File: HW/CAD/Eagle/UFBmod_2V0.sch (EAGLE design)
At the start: 67 parts, among them U301 MAX5217, U401 AT86RF215-ZU, U411 ASVTX-13-D-26.000MHZ-I05-T, U511 PE4259, U521 RFX1010, U581 B39871B3440U410, X1 TTE_EN11-HSM, X591 ANTENNATINY, X595 ANTENNATINY, X711 MOLEX 105017-0001, X721 PHOENIX_1990067_1X8X2MM50_PTS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, X722 PHOENIX_1990067_1X8X2MM50_PTS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, X723 PHOENIX_1990067_1X8X2MM50_PTS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

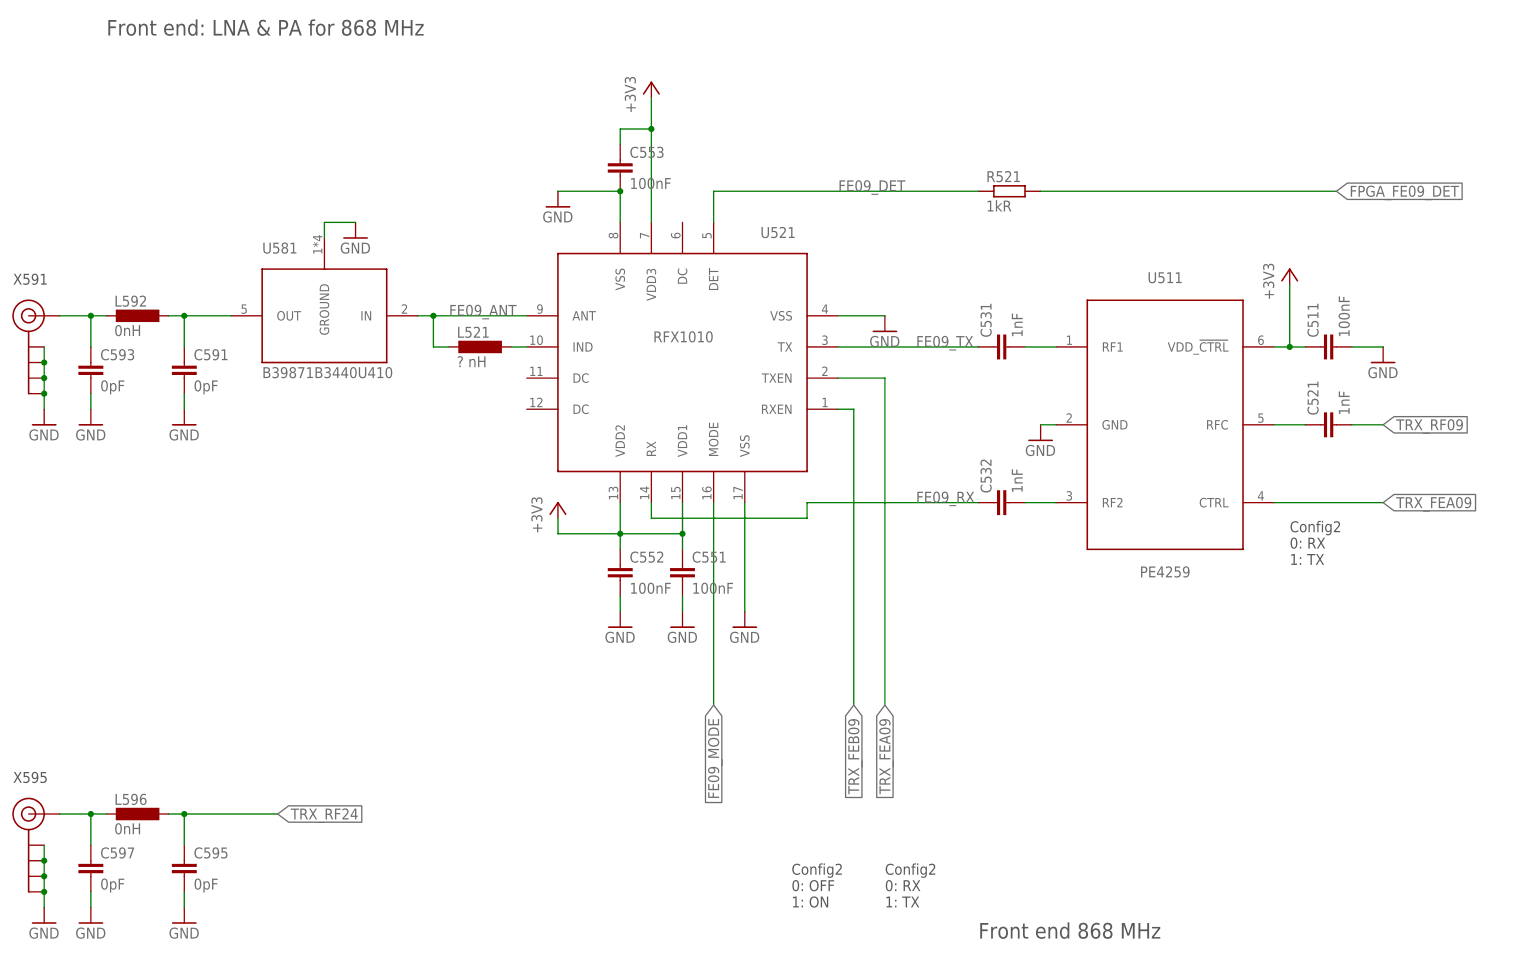
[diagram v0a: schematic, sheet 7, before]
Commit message: HW_2V0 - HW/CAD/Eagle - RFX1010 application schematic adapted
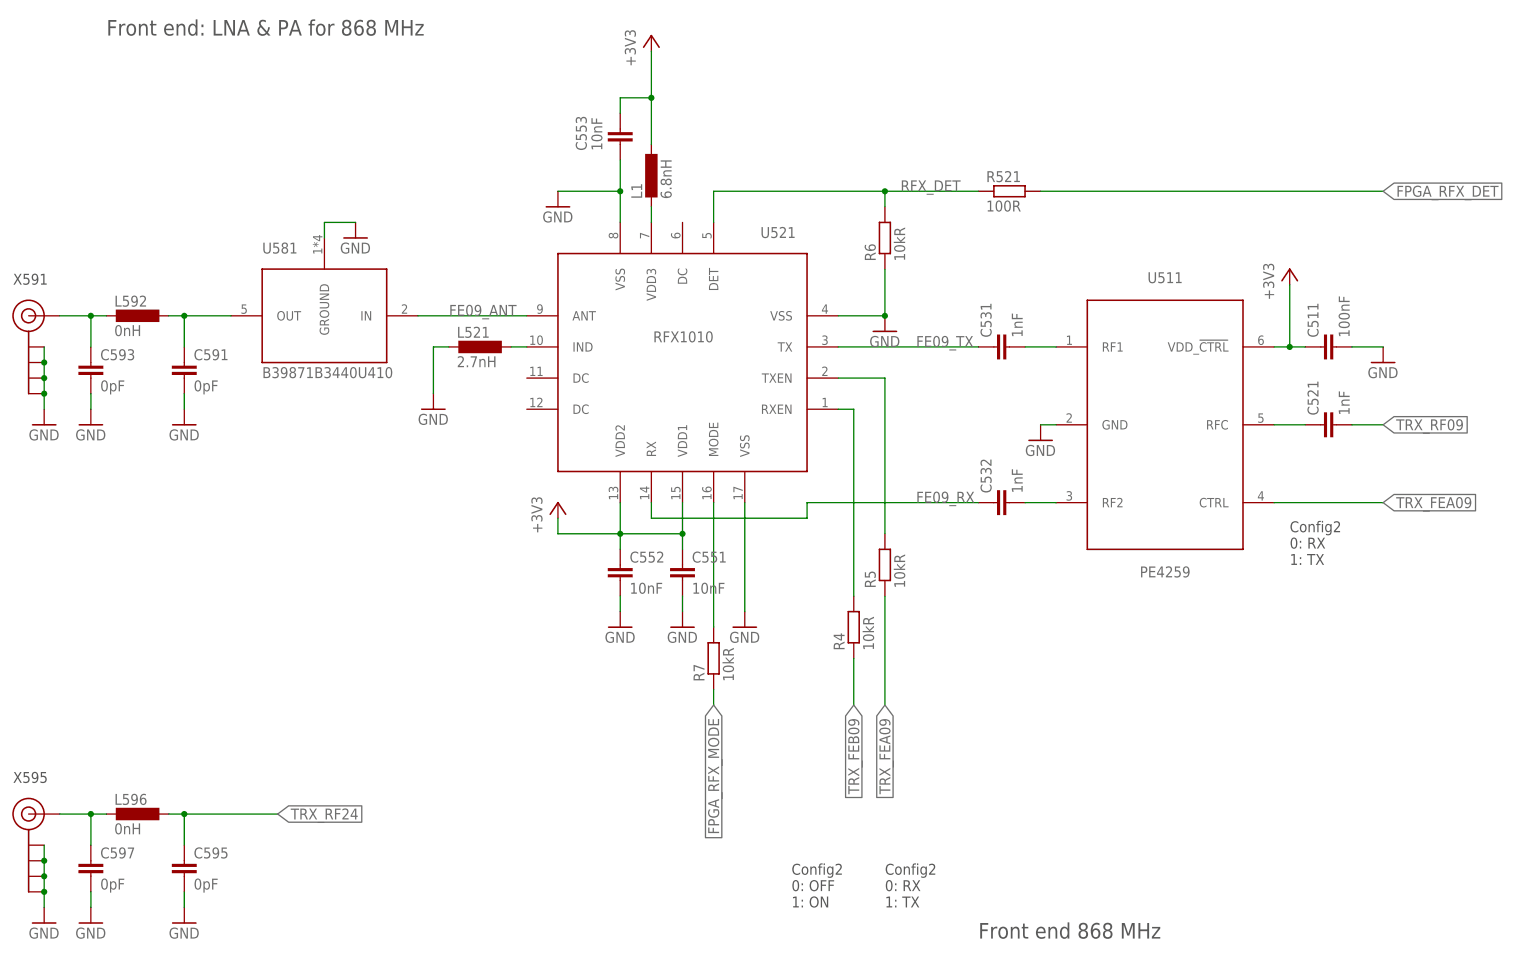
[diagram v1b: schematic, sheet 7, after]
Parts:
- added L1: 6.8nH, df4iah_rcl:L-EUL0603
- added R4, R5, R6, R7: 10kR, df4iah_rcl:R-EU_R0402
- C551, C552, C553: value 100nF -> 10nF
- L521: value ? nH -> 2.7nH
- R521: value 1kR -> 100R
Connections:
- net FE09_IND renamed RFX_IND
- net FPGA_FE09_DET renamed FPGA_RFX_DET
- removed net FE09_DET: R521.1, U521.DET
- removed net FE09_MODE: U521.MODE
- new net FPGA_RFX_MODE: R7.1
- new net RFX_DET: R521.1, R6.2, U521.DET
- new net RFX_MODE: R7.2, U521.MODE
- new net RFX_RXEN: R4.2, U521.RXEN
- new net RFX_TXEN: R5.2, U521.TXEN
- new net RFX_VDD3: L1.2, U521.VDD3
- net +3V3: now also L1.1; no longer U521.VDD3
- net FE09_ANT: no longer L521.2
- net GND: now also L521.2, R6.1
- net TRX_FEA09: now also R5.1; no longer U521.TXEN
- net TRX_FEB09: now also R4.1; no longer U521.RXEN
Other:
- note added: "SAMTEC LSHM-130-04.0-L-DV-A-S-K-TR 60 POS"
- note added: "SAMTEC LSHM-150-04.0-L-DV-A-S-K-TR 100 POS"
- moved on the sheet: C553

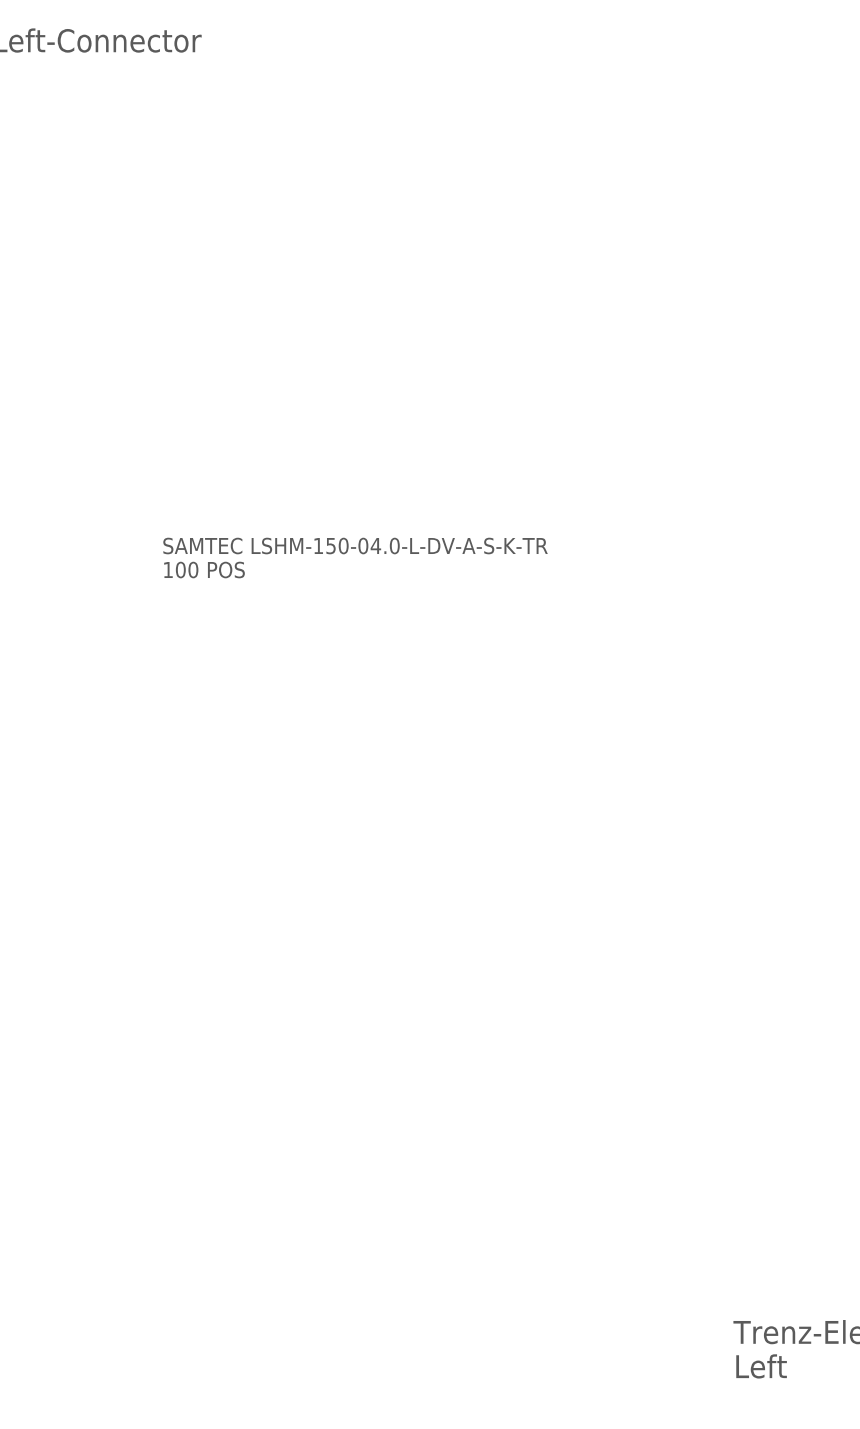
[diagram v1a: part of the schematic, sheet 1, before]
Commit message: HW_2V0 - HW/CAD/Eagle/lbr - df4iah_connector.lbr SEMTEC LSHM-150-02.5-L-DV-A-S-K-TR and LSHM-130-02.5-L-DV-A-S-K-TR added
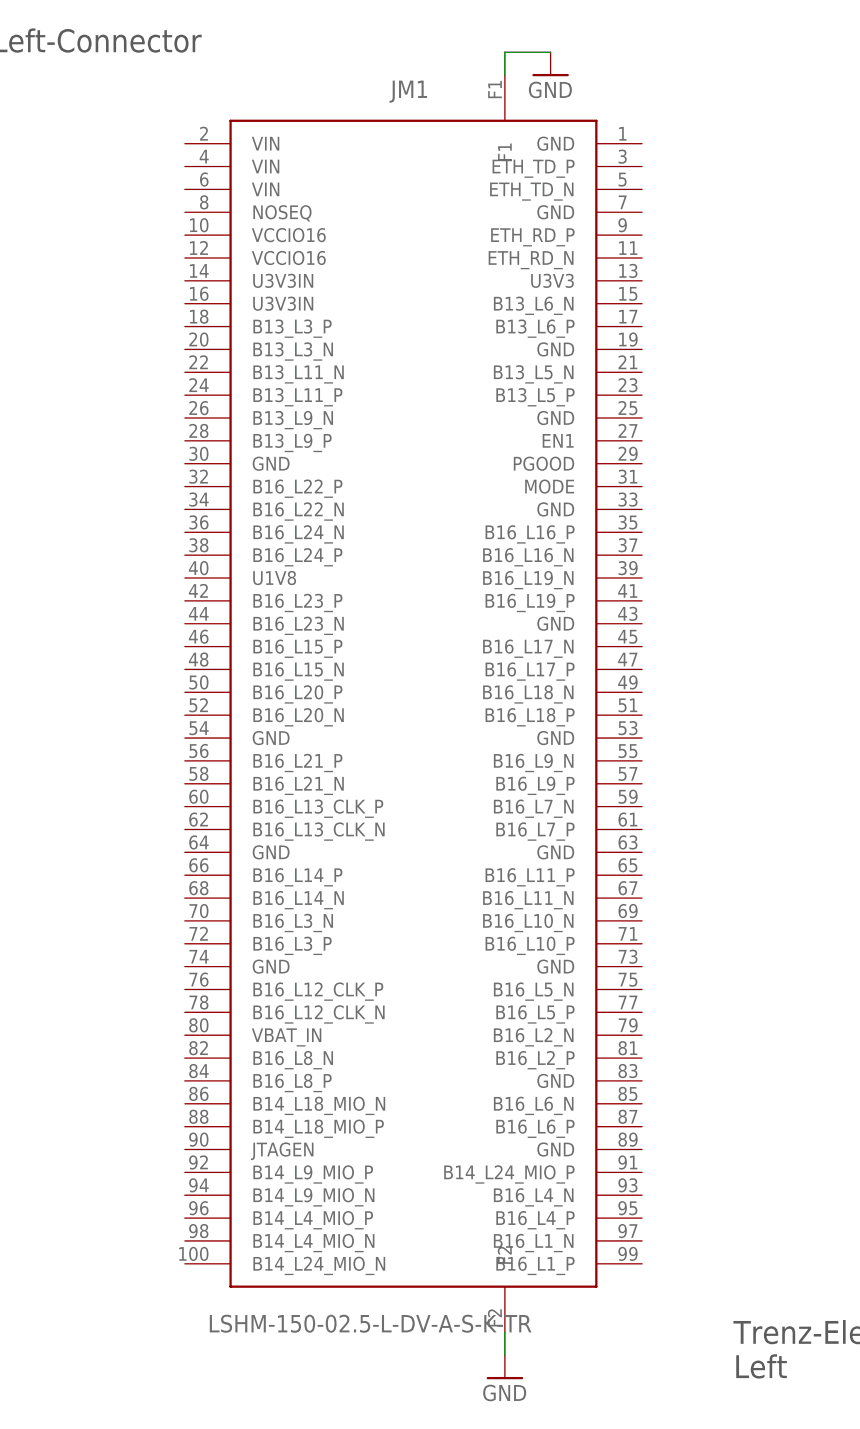
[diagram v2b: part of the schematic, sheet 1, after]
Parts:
- added JM1: LSHM-150-02.5-L-DV-A-S-K-TR, df4iah_connector:SAMTEC_LSHM-150-DV_JM1
- added JM2: LSHM-150-02.5-L-DV-A-S-K-TR, df4iah_connector:SAMTEC_LSHM-150-DV_JM2
- added JM3: LSHM-130-02.5-L-DV-A-S-K-TR, df4iah_connector:SAMTEC_LSHM-130-DV_JM3
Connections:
- net GND: now also JM1.F1, JM1.F2
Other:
- note removed: "SAMTEC LSHM-130-04.0-L-DV-A-S-K-TR 60 POS"
- note removed: "SAMTEC LSHM-150-04.0-L-DV-A-S-K-TR 100 POS"
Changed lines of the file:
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@@
 <part name="GND3" library="df4iah_supply" deviceset="GND" device=""/>
 <part name="R7" library="df4iah_rcl" deviceset="R-EU_" device="R0402" value="10kR"/>
+<part name="JM1" library="df4iah_connector" deviceset="SAMTEC_LSHM-150-DV_JM1" device="" value="LSHM-150-02.5-L-DV-A-S-K-TR"/>
+<part name="JM2" library="df4iah_connector" deviceset="SAMTEC_LSHM-150-DV_JM2" device="" value="LSHM-150-02.5-L-DV-A-S-K-TR"/>
+<part name="JM3" library="df4iah_connector" deviceset="SAMTEC_LSHM-130-DV_JM3" device="" value="LSHM-130-02.5-L-DV-A-S-K-TR"/>
+<part name="GND4" library="df4iah_supply" deviceset="GND" device=""/>
+<part name="GND5" library="df4iah_supply" deviceset="GND" device=""/>
 </parts>
 <sheets>
@@
 Left</text>
 <text x="22.86" y="162.56" size="2.54" layer="97" ratio="15">Trenz-Electronic TE0712-02-100-2C3  Left-Connector</text>
-<text x="101.6" y="104.14" size="1.778" layer="97">SAMTEC LSHM-150-04.0-L-DV-A-S-K-TR
-100 POS</text>
 </plain>
 <instances>
@@
 <attribute name="SHEET" x="230.505" y="5.08" size="2.54" layer="94" font="vector"/>
 </instance>
+<instance part="JM1" gate="G$1" x="129.54" y="91.44"/>
+<instance part="GND4" gate="1" x="144.78" y="160.02"/>
+<instance part="GND5" gate="1" x="139.7" y="15.24"/>
 </instances>
 <busses>
 </busses>
 <nets>
+<net name="GND" class="0">
+<segment>
+<pinref part="GND5" gate="1" pin="GND"/>
+<pinref part="JM1" gate="G$1" pin="F2"/>
+<wire x1="139.7" y1="17.78" x2="139.7" y2="20.32" width="0.1524" layer="91"/>
+</segment>
+<segment>
+<pinref part="GND4" gate="1" pin="GND"/>
+<wire x1="144.78" y1="162.56" x2="139.7" y2="162.56" width="0.1524" layer="91"/>
+<pinref part="JM1" gate="G$1" pin="F1"/>
+<wire x1="139.7" y1="162.56" x2="139.7" y2="160.02" width="0.1524" layer="91"/>
+</segment>
+</net>
 </nets>
 </sheet>
@@
 <text x="165.1" y="15.24" size="2.54" layer="97" ratio="15">Trenz-Electronic FPGA
 Right</text>
-<text x="101.6" y="104.14" size="1.778" layer="97">SAMTEC LSHM-150-04.0-L-DV-A-S-K-TR
-100 POS</text>
 </plain>
 <instances>
@@
 <attribute name="SHEET" x="230.505" y="5.08" size="2.54" layer="94" font="vector"/>
 </instance>
+<instance part="JM2" gate="G$1" x="129.54" y="91.44"/>
 </instances>
 <busses>
@@
 <text x="165.1" y="15.24" size="2.54" layer="97" ratio="15">Trenz-Electronic FPGA
 Top</text>
-<text x="101.6" y="104.14" size="1.778" layer="97">SAMTEC LSHM-130-04.0-L-DV-A-S-K-TR
-60 POS</text>
 </plain>
 <instances>
@@
 <attribute name="SHEET" x="230.505" y="5.08" size="2.54" layer="94" font="vector"/>
 </instance>
+<instance part="JM3" gate="G$1" x="129.54" y="91.44"/>
 </instances>
 <busses>

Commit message: HW_2V0 - HW/CAD/Eagle/lbr - df4iah_connector.lbr SEMTEC LSHM-150-02.5-L-DV-A-S-K-TR and LSHM-130-02.5-L-DV-A-S-K-TR fixed
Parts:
- removed JM1: LSHM-150-02.5-L-DV-A-S-K-TR, df4iah_connector:SAMTEC_LSHM-150-DV_JM1
- removed JM2: LSHM-150-02.5-L-DV-A-S-K-TR, df4iah_connector:SAMTEC_LSHM-150-DV_JM2
- removed JM3: LSHM-130-02.5-L-DV-A-S-K-TR, df4iah_connector:SAMTEC_LSHM-130-DV_JM3
- added JB1: (no value), df4iah_connector:SAMTEC_LSHM-150-DV_JB1
- added JB2: (no value), df4iah_connector:SAMTEC_LSHM-150-DV_JB2
- added JB3: (no value), df4iah_connector:SAMTEC_LSHM-130-DV_JB3
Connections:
- net GND: now also JB1.F1, JB1.F2, JB2.F1, JB2.F2, JB3.F1, JB3.F2; no longer JM1.F1, JM1.F2
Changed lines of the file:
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@@
 </attributes>
 <variantdefs>
-<variantdef name="Max"/>
 <variantdef name="Std"/>
 </variantdefs>
@@
 <part name="GND3" library="df4iah_supply" deviceset="GND" device=""/>
 <part name="R7" library="df4iah_rcl" deviceset="R-EU_" device="R0402" value="10kR"/>
-<part name="JM1" library="df4iah_connector" deviceset="SAMTEC_LSHM-150-DV_JM1" device="" value="LSHM-150-02.5-L-DV-A-S-K-TR"/>
-<part name="JM2" library="df4iah_connector" deviceset="SAMTEC_LSHM-150-DV_JM2" device="" value="LSHM-150-02.5-L-DV-A-S-K-TR"/>
-<part name="JM3" library="df4iah_connector" deviceset="SAMTEC_LSHM-130-DV_JM3" device="" value="LSHM-130-02.5-L-DV-A-S-K-TR"/>
 <part name="GND4" library="df4iah_supply" deviceset="GND" device=""/>
 <part name="GND5" library="df4iah_supply" deviceset="GND" device=""/>
+<part name="GND6" library="df4iah_supply" deviceset="GND" device=""/>
+<part name="GND7" library="df4iah_supply" deviceset="GND" device=""/>
+<part name="JB1" library="df4iah_connector" deviceset="SAMTEC_LSHM-150-DV_JB1" device=""/>
+<part name="JB2" library="df4iah_connector" deviceset="SAMTEC_LSHM-150-DV_JB2" device=""/>
+<part name="JB3" library="df4iah_connector" deviceset="SAMTEC_LSHM-130-DV_JB3" device=""/>
+<part name="GND8" library="df4iah_supply" deviceset="GND" device=""/>
+<part name="GND9" library="df4iah_supply" deviceset="GND" device=""/>
 </parts>
 <sheets>
@@
 <attribute name="SHEET" x="230.505" y="5.08" size="2.54" layer="94" font="vector"/>
 </instance>
-<instance part="JM1" gate="G$1" x="129.54" y="91.44"/>
 <instance part="GND4" gate="1" x="144.78" y="160.02"/>
 <instance part="GND5" gate="1" x="139.7" y="15.24"/>
+<instance part="JB1" gate="G$1" x="129.54" y="91.44"/>
 </instances>
 <busses>
@@
 <segment>
 <pinref part="GND5" gate="1" pin="GND"/>
-<pinref part="JM1" gate="G$1" pin="F2"/>
 <wire x1="139.7" y1="17.78" x2="139.7" y2="20.32" width="0.1524" layer="91"/>
+<pinref part="JB1" gate="G$1" pin="F2"/>
 </segment>
 <segment>
 <pinref part="GND4" gate="1" pin="GND"/>
 <wire x1="144.78" y1="162.56" x2="139.7" y2="162.56" width="0.1524" layer="91"/>
-<pinref part="JM1" gate="G$1" pin="F1"/>
 <wire x1="139.7" y1="162.56" x2="139.7" y2="160.02" width="0.1524" layer="91"/>
+<pinref part="JB1" gate="G$1" pin="F1"/>
 </segment>
 </net>
@@
 <attribute name="SHEET" x="230.505" y="5.08" size="2.54" layer="94" font="vector"/>
 </instance>
-<instance part="JM2" gate="G$1" x="129.54" y="91.44"/>
+<instance part="GND6" gate="1" x="144.78" y="160.02"/>
+<instance part="GND7" gate="1" x="139.7" y="15.24"/>
+<instance part="JB2" gate="G$1" x="129.54" y="91.44"/>
 </instances>
 <busses>
 </busses>
 <nets>
+<net name="GND" class="0">
+<segment>
+<pinref part="GND6" gate="1" pin="GND"/>
+<wire x1="144.78" y1="162.56" x2="139.7" y2="162.56" width="0.1524" layer="91"/>
+<wire x1="139.7" y1="162.56" x2="139.7" y2="160.02" width="0.1524" layer="91"/>
+<pinref part="JB2" gate="G$1" pin="F1"/>
+</segment>
+<segment>
+<pinref part="GND7" gate="1" pin="GND"/>
+<wire x1="139.7" y1="17.78" x2="139.7" y2="20.32" width="0.1524" layer="91"/>
+<pinref part="JB2" gate="G$1" pin="F2"/>
+</segment>
+</net>
 </nets>
 </sheet>
@@
 <attribute name="SHEET" x="230.505" y="5.08" size="2.54" layer="94" font="vector"/>
 </instance>
-<instance part="JM3" gate="G$1" x="129.54" y="91.44"/>
+<instance part="JB3" gate="G$1" x="129.54" y="91.44" rot="R90"/>
+<instance part="GND8" gate="1" x="83.82" y="96.52"/>
+<instance part="GND9" gate="1" x="177.8" y="96.52"/>
 </instances>
 <busses>
 </busses>
 <nets>
+<net name="GND" class="0">
+<segment>
+<pinref part="GND8" gate="1" pin="GND"/>
+<wire x1="83.82" y1="99.06" x2="83.82" y2="101.6" width="0.1524" layer="91"/>
+<wire x1="83.82" y1="101.6" x2="86.36" y2="101.6" width="0.1524" layer="91"/>
+<pinref part="JB3" gate="G$1" pin="F1"/>
+</segment>
+<segment>
+<pinref part="GND9" gate="1" pin="GND"/>
+<wire x1="177.8" y1="99.06" x2="177.8" y2="101.6" width="0.1524" layer="91"/>
+<wire x1="177.8" y1="101.6" x2="175.26" y2="101.6" width="0.1524" layer="91"/>
+<pinref part="JB3" gate="G$1" pin="F2"/>
+</segment>
+</net>
 </nets>
 </sheet>
